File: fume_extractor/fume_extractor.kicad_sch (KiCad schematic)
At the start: 18 parts, among them J1 Conn_01x04_MountingPin, J2 USB_C_Receptacle_USB2.0_16P, Q1 Q_NPN_BCE, U1 ATtiny1626-M

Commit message: rev 1
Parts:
- removed J1: Conn_01x04_MountingPin, Connector_PinHeader_2.54mm:PinHeader_1x04_P2.54mm_Vertical, symbol Connector_Generic_MountingPin:Conn_01x04_MountingPin
- removed Q1: Q_NPN_BCE, Package_TO_SOT_SMD:SOT-223-3_TabPin2, symbol Device:Q_NPN_BCE
- removed TP1, TP2, TP3, TP4, TP5, TP6: TestPoint, TestPoint:TestPoint_THTPad_D1.0mm_Drill0.5mm, symbol Connector:TestPoint
- added C2: 4.7 uF, Capacitor_SMD:C_0603_1608Metric, symbol Device:C
- added C3: 10 pF, Capacitor_SMD:C_0603_1608Metric, symbol Device:C
- added C4: 1 uF, Capacitor_SMD:C_0603_1608Metric, symbol Device:C
- added D1: D, Diode_SMD:D_SOD-123, symbol Device:D
- added J1, J3: Conn_01x04, Connector_PinHeader_2.54mm:PinHeader_1x04_P2.54mm_Vertical, symbol Connector_Generic:Conn_01x04
- added L1: 10 uH, unsurv_offline_pcb_footprints:CR32, symbol Device:L
- added U2: TPS61040DRV, Package_SON:WSON-6-1EP_2x2mm_P0.65mm_EP1x1.6mm, symbol Regulator_Switching:TPS61040DRV
- added U3: ~, unsurv_offline_pcb_footprints:testpoint_array_2x3, symbol unsurv_offline_pcb_symbols:testpoint_array_2x3
- R1: value 2.2k -> 100k
- R2: value 4.7k -> 866k
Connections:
- net +12V: now also R2.2, C3.1, C4.1, D1.1 (K), J3.3 (Pin_3); no longer R1.1
- net FAN_PWM: now also R3.2, R4.1, J3.1 (Pin_1); no longer R1.2
- net GND: now also R1.1, C2.2, C4.2, J1.4 (Pin_4), J3.4 (Pin_4), U2.1 (GND), U3.3 (GND), U3.6 (GND)
- net RX: now also U3.5 (RX)
- net SCL: now also U1.2 (PA3), J1.3 (Pin_3); no longer U1.14 (PB0)
- net SDA: now also U1.1 (PA2), J1.2 (Pin_2); no longer U1.13 (PB1)
- net TX: now also U3.4 (TX)
- net UPDI: now also U3.2 (UPDI)
- net FAN_RPM: now reaches U1.7 (PA6)
- net FAN_RPM: now also J3.2 (Pin_2)
- net VCC renamed +5V
- net +5V: now also C2.1, J1.1 (Pin_1), L1.1, U2.2 (VIN), U2.3 (EN), U3.1 (VCC)
- new net: C3.2, R1.2, R2.1, U2.4 (FB)
- new net: D1.2 (A), L1.2, U2.6 (SW)

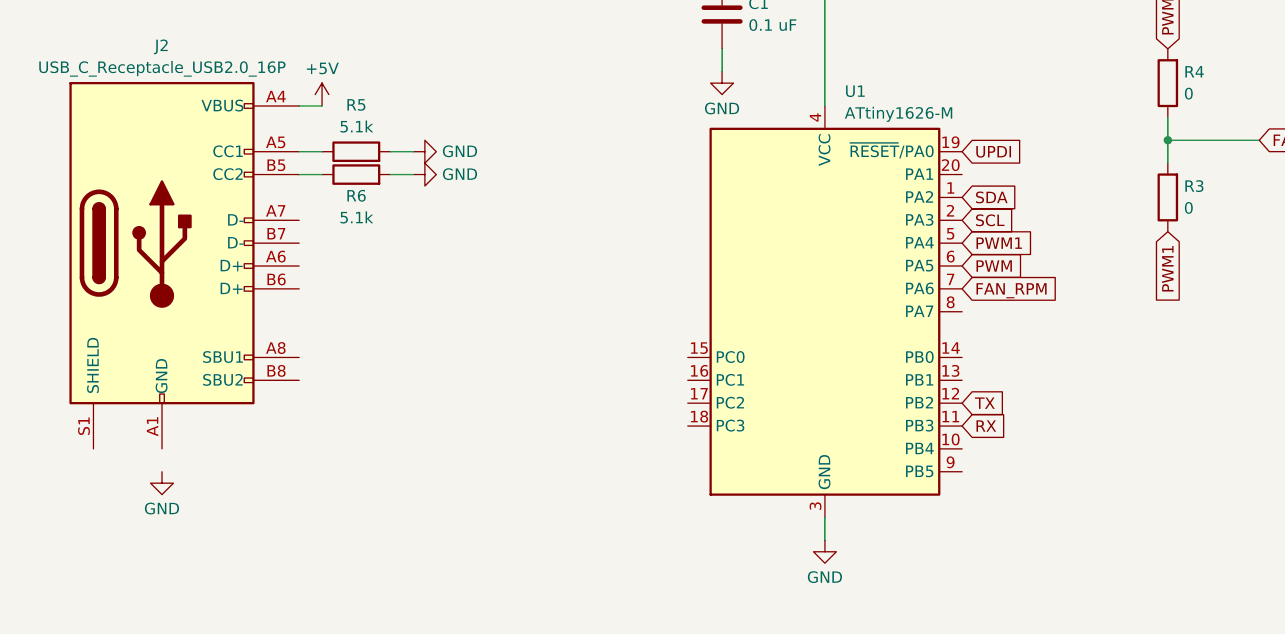
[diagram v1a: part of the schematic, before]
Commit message: fix GND connection on USB C
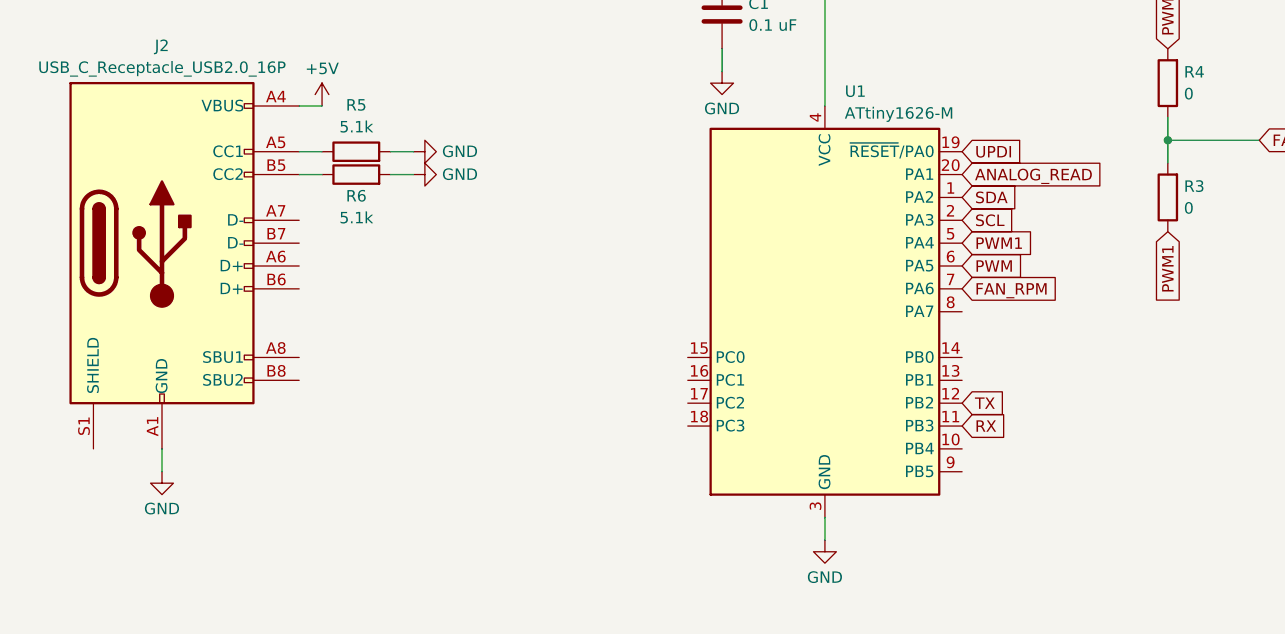
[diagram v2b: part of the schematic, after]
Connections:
- net ANALOG_READ: now also U1.20 (PA1)
- net GND: now also J2.A1 (GND), J2.A12 (GND), J2.B1 (GND), J2.B12 (GND)
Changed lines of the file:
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@@
+	(wire
+		(pts
+			(xy 46.99 93.98) (xy 46.99 96.52)
+		)
+		(stroke
+			(width 0)
+			(type default)
+		)
+	)
 	(wire
 		(pts
@@
 				(hide yes)
 			)
+		)
+	)
+	(global_label "ANALOG_READ"
+		(shape input)
+		(at 135.89 63.5 0)
+		(fields_autoplaced yes)
+		(effects
+			(font
+				(size 1.27 1.27)
+			)
+			(justify left)
+		)
+		(property "Intersheetrefs" "${INTERSHEET_REFS}"
+			(at 151.7567 63.5 0)
+			(effects
+				(font
+					(size 1.27 1.27)
+				)
+				(justify left)
+				(hide yes)
+			)
